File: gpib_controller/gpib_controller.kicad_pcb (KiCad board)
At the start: 2 copper layers, 2 parts, among them U2 SN75160BDW, U3 STM32H533RETx

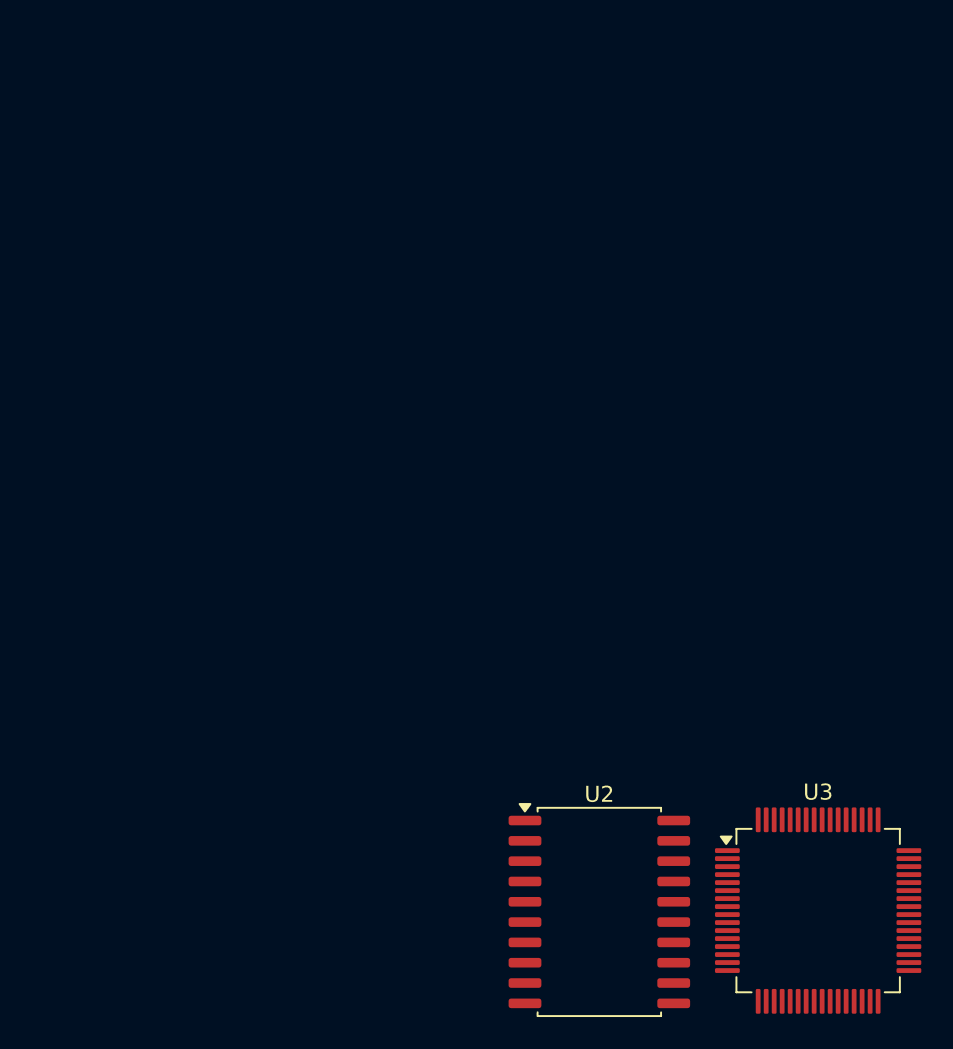
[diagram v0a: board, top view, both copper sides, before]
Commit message: Updated title block and structure
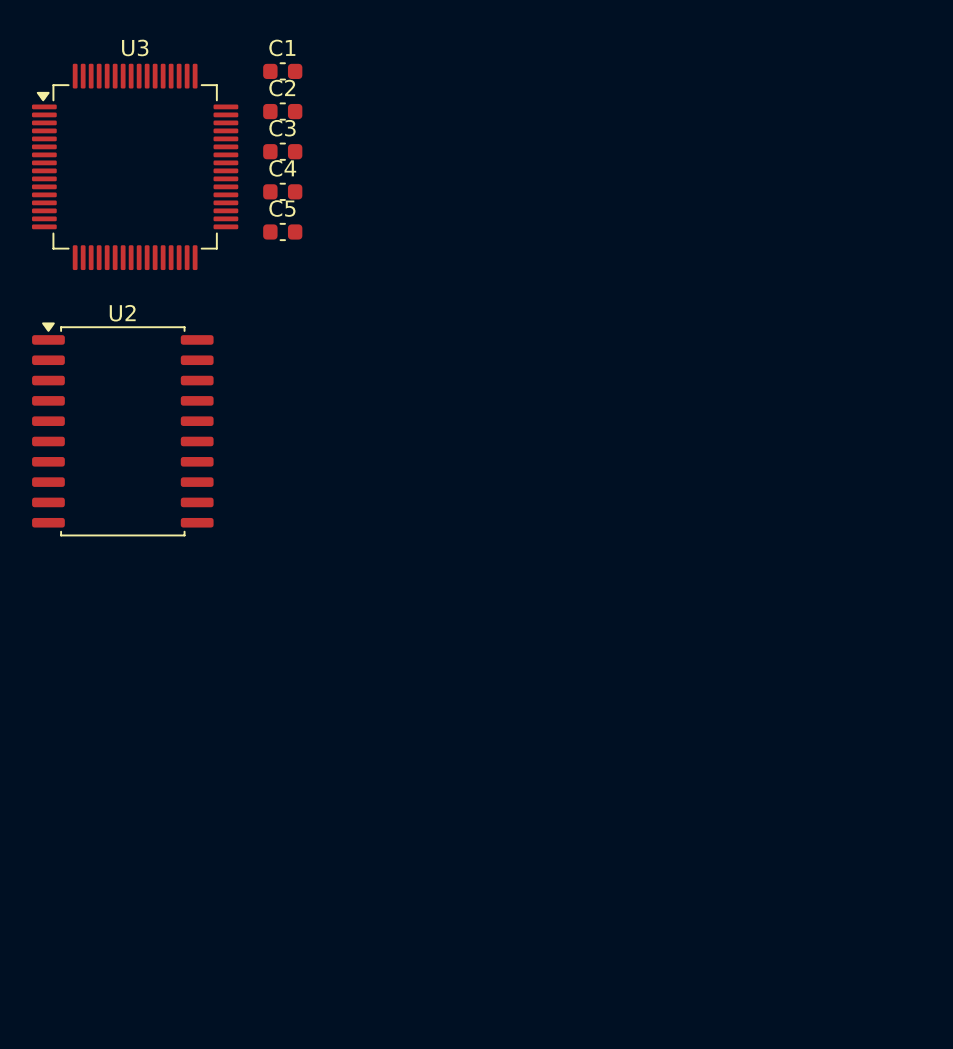
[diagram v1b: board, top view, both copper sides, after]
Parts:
- added C1: 100nF, Capacitor_SMD:C_0603_1608Metric, F.Cu at (107.3, 45.8)
- added C2: 100nF, Capacitor_SMD:C_0603_1608Metric, F.Cu at (107.3, 48.3)
- added C3: 100nF, Capacitor_SMD:C_0603_1608Metric, F.Cu at (107.3, 50.8)
- added C4: 100nF, Capacitor_SMD:C_0603_1608Metric, F.Cu at (107.3, 53.3)
- added C5: 4.7uF, Capacitor_SMD:C_0603_1608Metric, F.Cu at (107.3, 55.8)
- moved U3 63.1 mm to (98.1, 51.8)
- moved U2 42.3 mm to (97.3, 68.3)
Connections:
- U3 pad 19: unconnected-(U3A-VDD-Pad19) -> +3V3
- U3 pad 32: unconnected-(U3A-VDD-Pad32) -> +3V3
- U3 pad 48: unconnected-(U3A-VDD-Pad48) -> +3V3
- U3 pad 64: unconnected-(U3A-VDD-Pad64) -> +3V3
